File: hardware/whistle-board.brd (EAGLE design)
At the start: 75.9 x 21.7 mm, 15 parts, among them IC1 MCP4131, IC2 L272

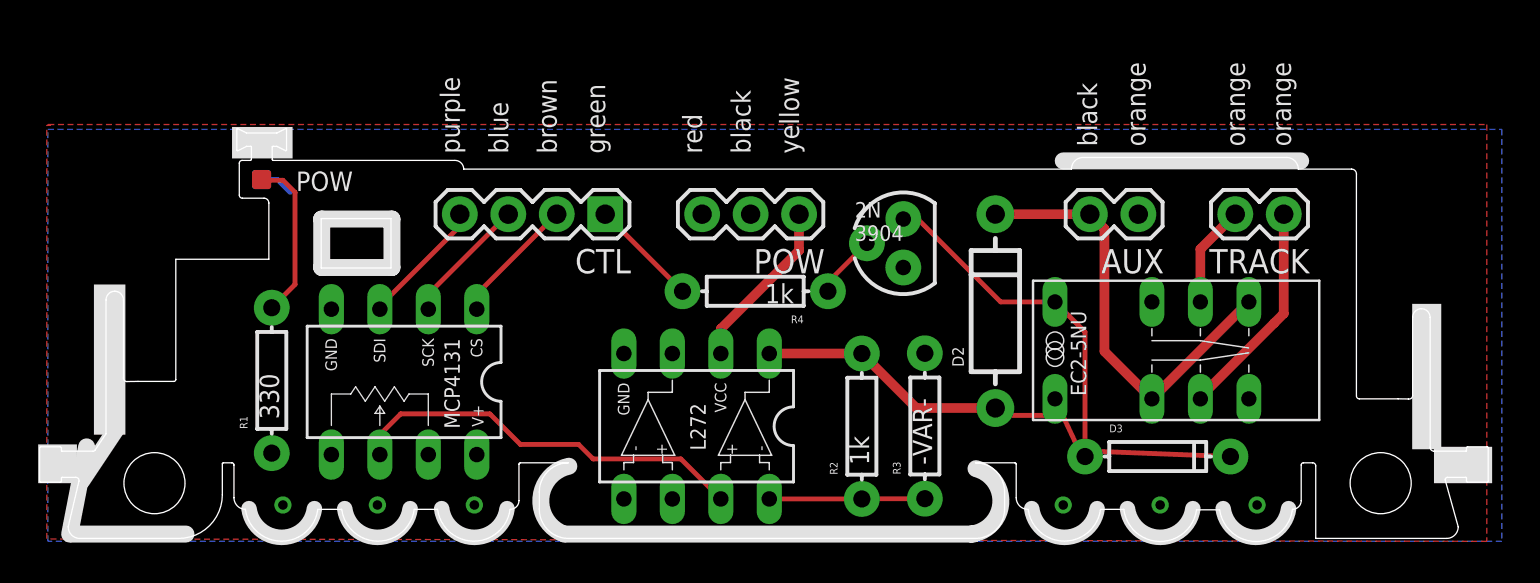
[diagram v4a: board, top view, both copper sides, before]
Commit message: changes after last fab
- removing opamp short to ground
- fixing missing silkscreen details
- small component moves
- adding support around left railing
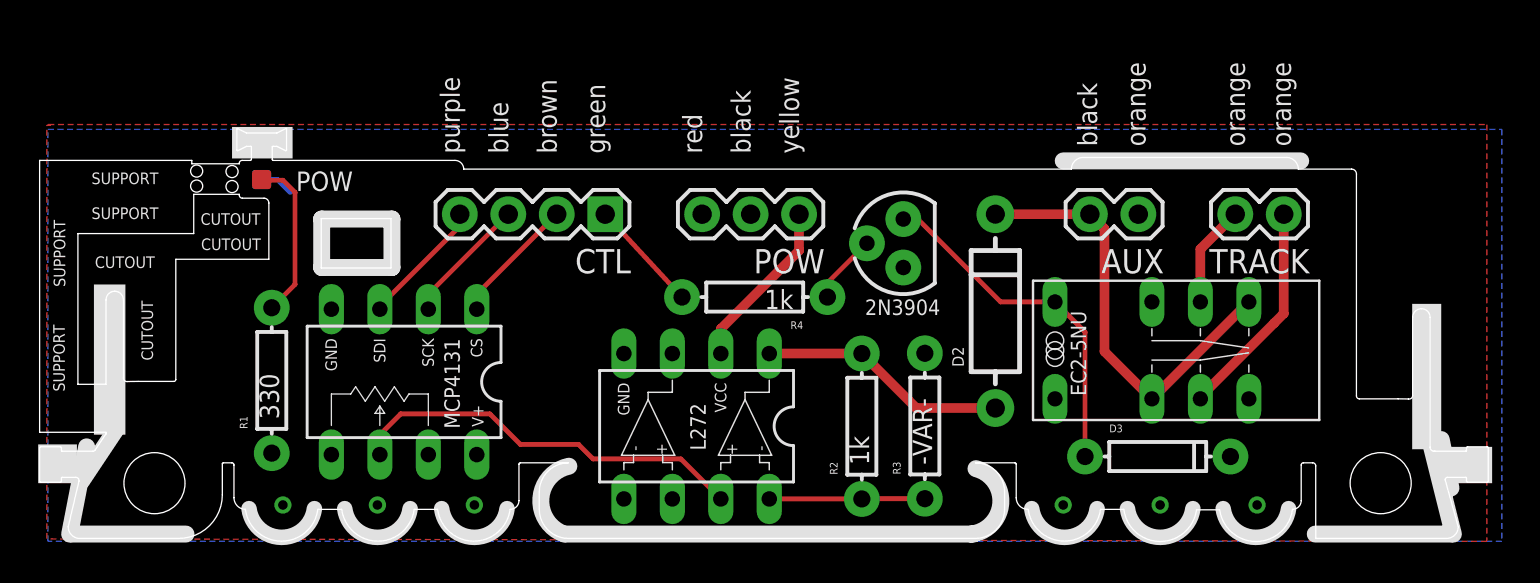
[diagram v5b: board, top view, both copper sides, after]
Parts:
- moved R4 0.31 mm to (37.0, 12.8)
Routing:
- net 5V: track 15.3 -> 0.00 mm
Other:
- outline, holes or cut-outs redrawn
- board text added: "2N3904"
- board text added: "CUTOUT"
- board text added: "SUPPORT"
- board text removed: "2N 3904"
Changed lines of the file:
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@@
 <setting verticaltext="up"/>
 </settings>
-<grid distance="0.005" unitdist="inch" unit="inch" style="lines" multiple="1" display="yes" altdistance="0.025" altunitdist="inch" altunit="inch"/>
+<grid distance="0.001" unitdist="inch" unit="inch" style="lines" multiple="1" display="yes" altdistance="0.025" altunitdist="inch" altunit="inch"/>
 <layers>
 <layer number="1" name="Top" color="4" fill="1" visible="yes" active="yes"/>
@@
 <layer number="27" name="tValues" color="7" fill="1" visible="yes" active="yes"/>
 <layer number="28" name="bValues" color="7" fill="1" visible="yes" active="yes"/>
-<layer number="29" name="tStop" color="7" fill="3" visible="yes" active="yes"/>
+<layer number="29" name="tStop" color="7" fill="3" visible="no" active="yes"/>
 <layer number="30" name="bStop" color="7" fill="6" visible="no" active="yes"/>
 <layer number="31" name="tCream" color="7" fill="4" visible="no" active="yes"/>
@@
 <layer number="43" name="vRestrict" color="2" fill="10" visible="yes" active="yes"/>
 <layer number="44" name="Drills" color="7" fill="1" visible="yes" active="yes"/>
-<layer number="45" name="Holes" color="7" fill="1" visible="no" active="yes"/>
+<layer number="45" name="Holes" color="7" fill="1" visible="yes" active="yes"/>
 <layer number="46" name="Milling" color="3" fill="1" visible="no" active="yes"/>
 <layer number="47" name="Measures" color="7" fill="1" visible="no" active="yes"/>
@@
 <wire x1="2.481053125" y1="4.78838125" x2="3.03946875" y2="5.626003125" width="0" layer="20"/>
 <wire x1="3.03946875" y1="5.626003125" x2="3.048" y2="5.65418125" width="0" layer="20" curve="33.68909"/>
-<wire x1="3.048" y1="5.65418125" x2="3.048" y2="12.6492" width="0" layer="20"/>
 <wire x1="3.048" y1="12.6492" x2="3.5052" y2="13.1064" width="0" layer="20" curve="-90"/>
 <wire x1="3.5052" y1="13.1064" x2="3.9624" y2="12.6492" width="0" layer="20" curve="-90"/>
@@
 <wire x1="65.024" y1="1.7145" x2="61.595" y2="1.7145" width="0.8128" layer="21" curve="-165.227914"/>
 <wire x1="10.181103125" y1="19.9644" x2="10.033" y2="19.816296875" width="0" layer="20" curve="90"/>
-<wire x1="10.033" y1="19.816296875" x2="10.033" y2="18.1458375" width="0" layer="20"/>
+<wire x1="10.033" y1="19.816296875" x2="10.033" y2="19.7866" width="0" layer="20"/>
+<wire x1="10.033" y1="18.1864" x2="10.033" y2="18.1458375" width="0" layer="20"/>
 <wire x1="10.033" y1="18.1458375" x2="10.1956375" y2="17.9832" width="0" layer="20" curve="90"/>
 <wire x1="10.1956375" y1="17.9832" x2="11.3284" y2="17.9832" width="0" layer="20"/>
@@
 <wire x1="72.644" y1="4.7244" x2="72.6948" y2="4.7244" width="0" layer="20"/>
 <text x="13.0048" y="18.3642" size="1.016" layer="21">POW</text>
-<wire x1="13.97" y1="1.7145" x2="10.541" y2="1.7145" width="0.8128" layer="30" curve="-165.227914"/>
-<wire x1="18.9865" y1="1.7145" x2="15.5575" y2="1.7145" width="0.8128" layer="30" curve="-165.227914"/>
-<wire x1="24.0665" y1="1.7145" x2="20.6375" y2="1.7145" width="0.8128" layer="30" curve="-165.227914"/>
-<wire x1="54.991" y1="1.7145" x2="51.562" y2="1.7145" width="0.8128" layer="30" curve="-165.227914"/>
-<wire x1="65.024" y1="1.7145" x2="61.595" y2="1.7145" width="0.8128" layer="30" curve="-165.227914"/>
-<wire x1="60.0075" y1="1.7145" x2="56.5785" y2="1.7145" width="0.8128" layer="30" curve="-165.227914"/>
 <text x="46.99" y="4.699" size="1.016" layer="22" rot="MR0">Whistle Board
 Version 1</text>
@@
 <text x="54.991" y="20.701" size="1.016" layer="25" rot="R90">black</text>
 <text x="57.531" y="20.701" size="1.016" layer="25" rot="R90">orange</text>
-<text x="42.291" y="15.748" size="0.8128" layer="21">2N
-3904</text>
+<text x="42.8244" y="11.8618" size="0.8128" layer="21">2N3904</text>
 <rectangle x1="2.413" y1="5.588" x2="4.064" y2="13.462" layer="21"/>
 <rectangle x1="-0.508" y1="3.048" x2="1.524" y2="5.08" layer="21"/>
@@
 <wire x1="27.051" y1="0.381" x2="48.387" y2="0.381" width="0.889" layer="22"/>
 <wire x1="48.387" y1="0.381" x2="48.514" y2="0.381" width="0.889" layer="22"/>
+<wire x1="73.533" y1="0.381" x2="66.421" y2="0.381" width="0.889" layer="21"/>
+<wire x1="73.66" y1="0.381" x2="72.517" y2="4.953" width="0.889" layer="21"/>
+<wire x1="73.533" y1="2.794" x2="73.025" y2="5.334" width="0.889" layer="21"/>
+<wire x1="13.97" y1="1.7145" x2="10.541" y2="1.7145" width="0.8128" layer="22" curve="-165.227914"/>
+<wire x1="18.9865" y1="1.7145" x2="15.5575" y2="1.7145" width="0.8128" layer="22" curve="-165.227914"/>
+<wire x1="24.0665" y1="1.7145" x2="20.6375" y2="1.7145" width="0.8128" layer="22" curve="-165.227914"/>
+<wire x1="54.991" y1="1.7145" x2="51.562" y2="1.7145" width="0.8128" layer="22" curve="-165.227914"/>
+<wire x1="60.0075" y1="1.7145" x2="56.5785" y2="1.7145" width="0.8128" layer="22" curve="-165.227914"/>
+<wire x1="65.024" y1="1.7145" x2="61.595" y2="1.7145" width="0.8128" layer="22" curve="-165.227914"/>
+<hole x="2.794" y="7.874" drill="0.635"/>
+<hole x="2.794" y="6.985" drill="0.635"/>
+<hole x="2.794" y="6.096" drill="0.635"/>
+<wire x1="3.048" y1="12.6492" x2="3.048" y2="8.2296" width="0" layer="20"/>
+<wire x1="3.048" y1="8.2296" x2="1.5748" y2="8.2296" width="0" layer="20"/>
+<wire x1="3.048" y1="5.6388" x2="3.048" y2="5.715" width="0" layer="20"/>
+<wire x1="3.048" y1="5.715" x2="-0.4318" y2="5.715" width="0" layer="20"/>
+<wire x1="-0.4318" y1="5.715" x2="-0.4318" y2="19.9644" width="0" layer="20"/>
+<wire x1="-0.4318" y1="19.9644" x2="7.5438" y2="19.9644" width="0" layer="20"/>
+<hole x="9.652" y="19.3802" drill="0.635"/>
+<hole x="9.652" y="18.5928" drill="0.635"/>
+<wire x1="7.5438" y1="19.9644" x2="7.5438" y2="19.7866" width="0" layer="20"/>
+<wire x1="7.5438" y1="19.7866" x2="10.033" y2="19.7866" width="0" layer="20"/>
+<wire x1="10.033" y1="18.1864" x2="7.6454" y2="18.1864" width="0" layer="20"/>
+<hole x="7.7978" y="19.4056" drill="0.635"/>
+<hole x="7.7978" y="18.6182" drill="0.635"/>
+<wire x1="1.5748" y1="8.2296" x2="1.5748" y2="16.129" width="0" layer="20"/>
+<wire x1="1.5748" y1="16.129" x2="7.6454" y2="16.129" width="0" layer="20"/>
+<wire x1="7.6454" y1="16.129" x2="7.6454" y2="18.1864" width="0" layer="20"/>
+<text x="8.001" y="16.5862" size="0.6096" layer="21">CUTOUT</text>
+<text x="8.0264" y="15.2654" size="0.6096" layer="21">CUTOUT</text>
+<text x="2.4638" y="14.3256" size="0.6096" layer="21">CUTOUT</text>
+<text x="2.286" y="18.7198" size="0.6096" layer="21">SUPPORT</text>
+<text x="2.286" y="16.891" size="0.6096" layer="21">SUPPORT</text>
+<text x="0.9144" y="13.335" size="0.6096" layer="21" rot="R90">SUPPORT</text>
+<text x="0.889" y="7.8486" size="0.6096" layer="21" rot="R90">SUPPORT</text>
+<text x="5.5118" y="9.4742" size="0.6096" layer="21" rot="R90">CUTOUT</text>
 </plain>
 <attributes>
@@
 <attribute name="PROD_ID" value="RES-08380" x="90.4113" y="33.9852" size="1.778" layer="27" rot="R90" display="off"/>
 </element>
-<element name="R4" library="SparkFun-Resistors" package="AXIAL-0.3" value="1k" x="37.0713" y="13.1064" rot="R180">
-<attribute name="VALE" value="1k" x="-1.0287" y="57.5564" size="1.778" layer="27" rot="R180" display="off"/>
-<attribute name="PROD_ID" value="RES-08380" x="-1.0287" y="57.5564" size="1.778" layer="27" rot="R180" display="off"/>
+<element name="R4" library="SparkFun-Resistors" package="AXIAL-0.3" value="1k" x="37.0459" y="12.8016" rot="R180">
+<attribute name="VALE" value="1k" x="-1.0541" y="57.2516" size="1.778" layer="27" rot="R180" display="off"/>
+<attribute name="PROD_ID" value="RES-08380" x="-1.0541" y="57.2516" size="1.778" layer="27" rot="R180" display="off"/>
 </element>
 <element name="S1" library="custom-parts" package="EC2-5NU" value="EC2-5NU" x="59.1312" y="10.0076"/>
@@
 <contactref element="S1" pad="+"/>
 <contactref element="D3" pad="C"/>
-<wire x1="61.976" y1="4.445" x2="54.0512" y2="4.7498" width="0.254" layer="1"/>
-<wire x1="54.0512" y1="4.7498" x2="52.7812" y2="7.4676" width="0.254" layer="1"/>
-<wire x1="49.784" y1="6.604" x2="53.1876" y2="6.604" width="0.254" layer="1"/>
-<wire x1="53.1876" y1="6.604" x2="52.7812" y2="7.4676" width="0.254" layer="1"/>
 </signal>
 <signal name="GND">
@@
 <contactref element="CTL" pad="1"/>
 <wire x1="29.21" y1="17.145" x2="29.2227" y2="17.145" width="0.254" layer="1"/>
-<wire x1="29.2227" y1="17.145" x2="33.2613" y2="13.1064" width="0.254" layer="1"/>
+<wire x1="29.2227" y1="17.145" x2="33.2359" y2="12.8016" width="0.254" layer="1"/>
 </signal>
 <signal name="LEFT">
@@
 <contactref element="Q1" pad="2"/>
 <contactref element="R4" pad="P$1"/>
-<wire x1="40.8813" y1="13.1064" x2="40.8813" y2="13.5763" width="0.254" layer="1"/>
+<wire x1="40.8559" y1="12.8016" x2="40.8813" y2="13.5763" width="0.254" layer="1"/>
 <wire x1="40.8813" y1="13.5763" x2="42.926" y2="15.621" width="0.254" layer="1"/>
 </signal>
